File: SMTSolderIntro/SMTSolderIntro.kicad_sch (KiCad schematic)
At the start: 135 parts

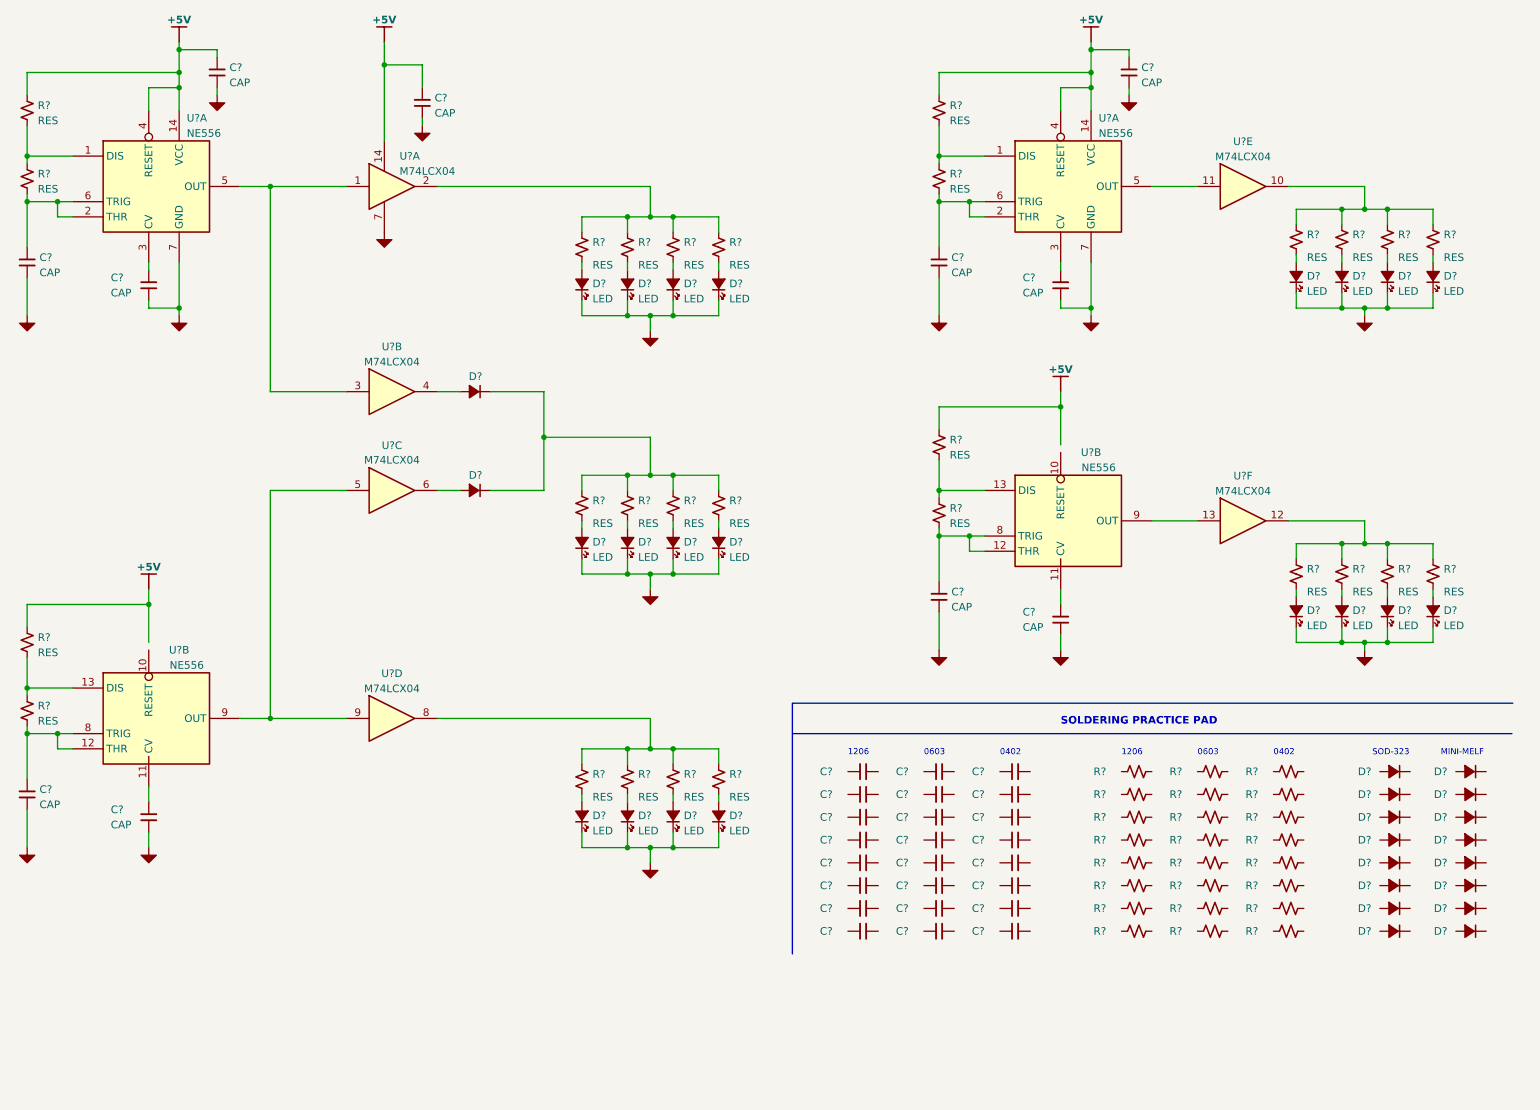
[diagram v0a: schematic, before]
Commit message: All components imported to board, nets still need work
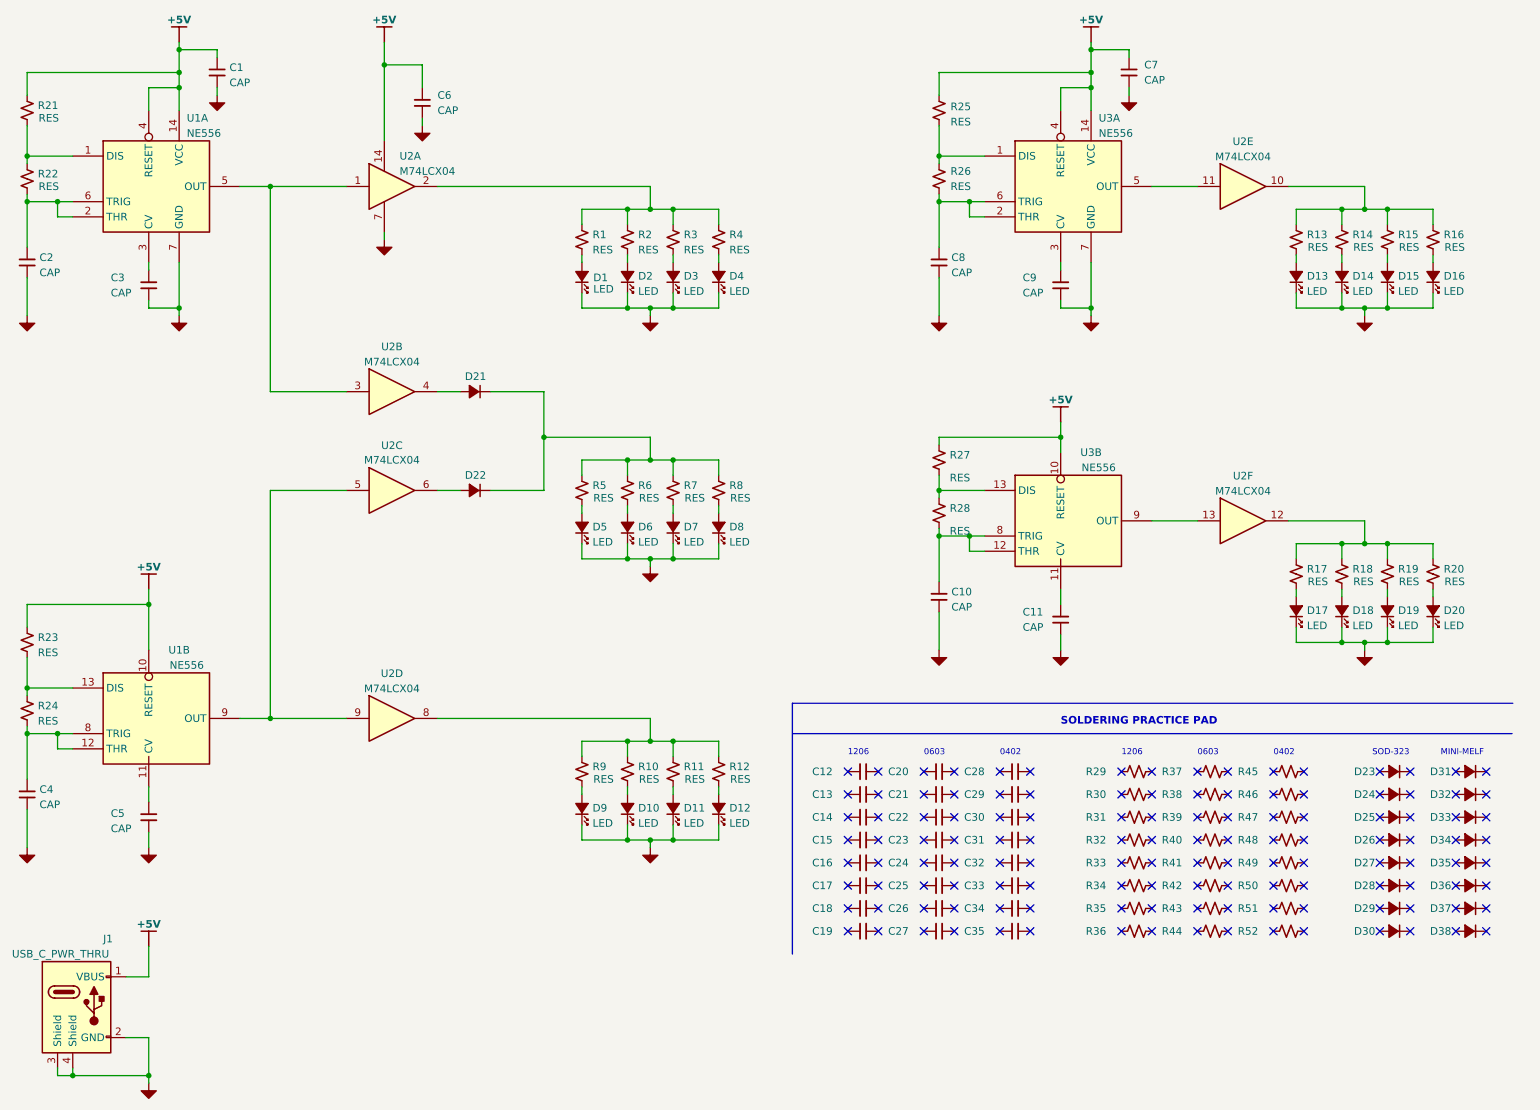
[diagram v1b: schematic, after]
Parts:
- removed D? (x2): DIODE, symbol Alpenglow:DIODE
- removed U? (x3): NE556, symbol Alpenglow:NE556
- added D21, D22: DIODE, Diode_SMD:D_MiniMELF_Handsoldering, symbol Alpenglow:DIODE
- added J1: USB_C_PWR_THRU, Alpenglow:USB_C_PWR_THRU, symbol Alpenglow:USB_C_PWR_THRU
- added U1: NE556, Alpenglow:SO-14, symbol Alpenglow:NE556
- added unit 2 of U3
- C1, C10, C11, C2, C3, C4, C5, C6, C7, C8, C9: renamed from C?; footprint (none) -> Capacitor_SMD:C_0805_2012Metric_Pad1.18x1.45mm_HandSolder
- C12, C13, C14, C15, C16, C17, C18, C19: renamed from C?; footprint (none) -> Capacitor_SMD:C_1206_3216Metric_Pad1.33x1.80mm_HandSolder
- C20, C21, C22, C23, C24, C25, C26, C27: renamed from C?; footprint (none) -> Capacitor_SMD:C_0603_1608Metric_Pad1.08x0.95mm_HandSolder
- C28, C29, C30, C31, C32, C33, C34, C35: renamed from C?; footprint (none) -> Capacitor_SMD:C_0402_1005Metric_Pad0.74x0.62mm_HandSolder
- D1, D10, D11, D12, D13, D14, D15, D16, D17, D18, D19, D2, D20, D3, D4, D5, D6, D7, D8, D9: renamed from D?; footprint (none) -> Alpenglow:LED_0805+; symbol Alpenglow:LED -> Alpenglow:LED_AK
- D23, D24, D25, D26, D27, D28, D29, D30: renamed from D?; footprint (none) -> Diode_SMD:D_SOD-323_HandSoldering
- D31, D32, D33, D34, D35, D36, D37, D38: renamed from D?; footprint (none) -> Diode_SMD:D_MiniMELF_Handsoldering
- R1, R10, R11, R12, R13, R14, R15, R16, R17, R18, R19, R2, R20, R21, R22, R23, R24, R25, R26, R27, R28, R3, R4, R5, R6, R7, R8, R9: renamed from R?; footprint (none) -> Resistor_SMD:R_0805_2012Metric_Pad1.20x1.40mm_HandSolder
- R29, R30, R31, R32, R33, R34, R35, R36: renamed from R?; footprint (none) -> Resistor_SMD:R_1206_3216Metric_Pad1.30x1.75mm_HandSolder
- R37, R38, R39, R40, R41, R42, R43, R44: renamed from R?; footprint (none) -> Resistor_SMD:R_0603_1608Metric_Pad0.98x0.95mm_HandSolder
- R45, R46, R47, R48, R49, R50, R51, R52: renamed from R?; footprint (none) -> Resistor_SMD:R_0402_1005Metric_Pad0.72x0.64mm_HandSolder
- U2: renamed from U?; footprint (none) -> Alpenglow:SO-16
- U3: renamed from U?; footprint (none) -> Alpenglow:SO-14
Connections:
- net +5V: now also C6.1, C7.1, R21.1, R25.1, R27.1, J1.1 (VBUS), U1.10 (RESET), U1.14 (VCC), U1.4 (RESET), U3.10 (RESET); no longer C2.1, C3.1, R1.1, R13.1, R2.1
- net GND: now also D1.K, D10.K, D11.K, D12.K, D13.K, D14.K, D15.K, D16.K, D17.K, D18.K, D19.K, D2.K, D20.K, D3.K, D4.K, D5.K, D6.K, D7.K, D8.K, D9.K, J1.2 (GND), J1.3 (Shield), J1.4 (Shield), U1.7 (GND); no longer D1.1 (K), D10.1 (K), D11.1 (K), D12.1 (K), D13.1 (K), D14.1 (K), D15.1 (K), D16.1 (K), D17.1 (K), D18.1 (K), D19.1 (K), D2.1 (K), D20.1 (K), D3.1 (K), D4.1 (K), D5.1 (K), D6.1 (K), D7.1 (K), D8.1 (K), D9.1 (K)
- net at U2.6: now also D22.A
- net at R14.1, R15.1, R16.1: now also R13.1, U2.10; no longer R17.1
- net at R19.1, R20.1, U2.12: now also R17.1, R18.1; no longer R21.1, R22.1
- net at R22.2: now also C2.1, U1.2 (THR), U1.6 (TRIG); no longer D16.2 (A)
- net at R17.2: now also D17.A; no longer D12.2 (A)
- net at R10.1, R11.1, R12.1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: now also U2.8; no longer U2.10
- net at R10.2: now also D10.A; no longer D6.2 (A)
- net at R21.2: now also R22.1, U1.1 (DIS); no longer D15.2 (A)
- net at U2.1, U2.3: now also U1.5 (OUT)
- net at R5.1, R6.1, R7.1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: now also D21.K, D22.K; no longer U2.2
- net at R12.2: now also D12.A; no longer D8.2 (A)
- net at U2.4: now also D21.A
- net at R15.2: now also D15.A; no longer D10.2 (A)
- net at U3.2 (THR), U3.6 (TRIG): now also C8.1, R26.2; no longer C5.1, R4.2
- net at U3.3 (CV): now also C9.1; no longer C7.1
- net at R24.2: now also C4.1, U1.12 (THR), U1.8 (TRIG); no longer C10.1
- net at R5.2: now also D5.A; no longer D1.2 (A)
- net at C11.1: now also U3.11 (CV)
- net at R23.2, R24.1: now also U1.13 (DIS)
- net at U2.5, U2.9: now also U1.9 (OUT)
- net at R11.2: now also D11.A; no longer D7.2 (A)
- net at R16.2: now also D16.A; no longer D11.2 (A)
- net at R9.2: now also D9.A; no longer D5.2 (A)
- net at R3.1: now also R1.1, R2.1, R4.1, U2.2; no longer R1.2
- net at R3.2: now also D3.A; no longer C4.1
- net at R20.2: now also D20.A; no longer D14.2 (A)
- net at R6.2: now also D6.A; no longer D2.2 (A)
- net at R18.2: now also D18.A; no longer C8.1
- net at R14.2: now also D14.A; no longer D9.2 (A)
- net at R28.2: now also C10.1, U3.12 (THR), U3.8 (TRIG); no longer D20.2 (A)
- net at R19.2: now also D19.A; no longer D13.2 (A)
- net at R13.2: now also D13.A; no longer R18.1
- net at R27.2: now also R28.1, U3.13 (DIS); no longer D19.2 (A)
- net at U2.13: now also U3.9 (OUT)
- net at R8.2: now also D8.A; no longer D4.2 (A)
- net at R7.2: now also D7.A; no longer D3.2 (A)
- net at R25.2: now also R26.1, U3.1 (DIS); no longer D17.2 (A)
- new net: D2.A, R2.2
- new net: C3.1, U1.3 (CV)
- new net: C5.1, U1.11 (CV)
- new net: D4.A, R4.2
- new net: D1.A, R1.2
- no-connect marks 0 -> 128
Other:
- moved on the sheet: C10, C11, C2, C3, C4, C5, C6, C7, C8, C9, D1, D10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

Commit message: fixed nets and components with bad footprints.  Ready for checking with printer.
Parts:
- D21, D22, D31, D32, D33, D34, D35, D36, D37, D38: footprint Diode_SMD:D_MiniMELF_Handsoldering -> Alpenglow:MINI_MELF
- D23, D24, D25, D26, D27, D28, D29, D30: footprint Diode_SMD:D_SOD-323_HandSoldering -> Alpenglow:SOD-323
- U2: footprint Alpenglow:SO-16 -> Alpenglow:SO-14

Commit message: Rough placement, added zip files to ignore
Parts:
- added D23, D24, D25, D26: DIODE, Alpenglow:SOD-323, symbol Alpenglow:DIODE
- added H1, H2, H3, H4: MountingHole_Pad, Alpenglow:MNTG-HOLE-BANANA, symbol Mechanical:MountingHole_Pad
- added J2: Barrel_Jack, Connector_BarrelJack:BarrelJack_CLIFF_FC681465S_SMT_Horizontal, symbol Connector:Barrel_Jack
- D21, D22: footprint Alpenglow:MINI_MELF -> Alpenglow:SOD-323
- renumbered D23 to D27, D24 to D28, D25 to D29, D26 to D30, D27 to D31, D28 to D32, D29 to D33, D30 to D34, D31 to D35, D32 to D36, D33 to D37, D34 to D38, D35 to D39, D36 to D40, D37 to D41, D38 to D42
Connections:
- net +5V: now also D23.K, D24.K, D25.K, D26.K; no longer J1.1 (VBUS)
- net GND: now also H1.1, H2.1, J2.2
- net BLINK1: now reaches R1.1, R2.1, R3.1, R4.1, U2.2
- net BLINK2: now reaches R10.1, R11.1, R12.1, R9.1, U2.8
- net CLK1: now reaches U1.5 (OUT), U2.1, U2.3
- net BLINK3: now reaches R13.1, R14.1, R15.1, R16.1, U2.10
- net CLK2: now reaches U1.9 (OUT), U2.5, U2.9
- net CLK3: now reaches U2.11, U3.5 (OUT)
- net BLINK5: now reaches D21.K, D22.K, R5.1, R6.1, R7.1, R8.1
- net BLINK4: now reaches R17.1, R18.1, R19.1, R20.1, U2.12
- net CLK4: now reaches U2.13, U3.9 (OUT)
- new net +Vbarrel: D26.A, J2.1
- new net +Vin_1: D23.A, H3.1
- new net +Vin_2: D24.A, H4.1
- new net +Vusb: D25.A, J1.1 (VBUS)
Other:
- note added: "MOUNTING HOLES / BANANA JACKS"
- moved on the sheet: J1

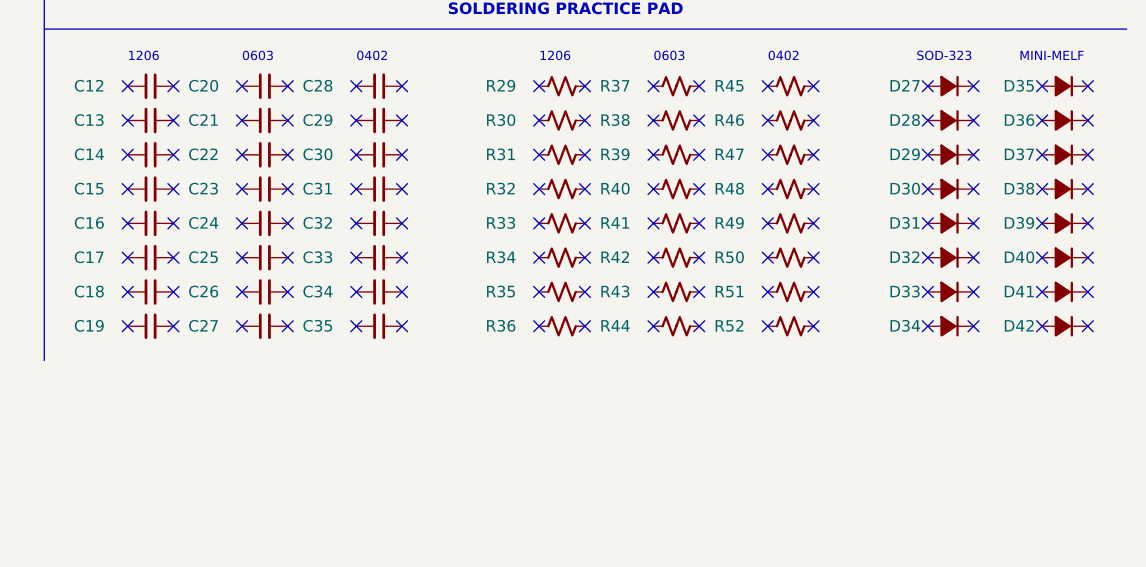
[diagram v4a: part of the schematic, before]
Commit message: Updated layout, Labeled practice component sizes, Added board name, Updated Schematic
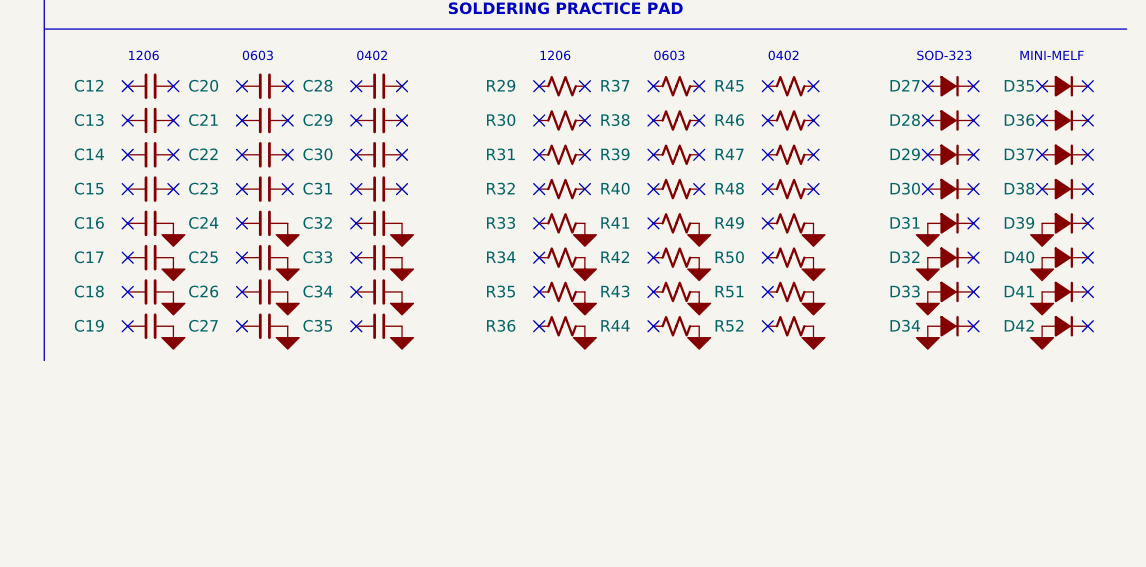
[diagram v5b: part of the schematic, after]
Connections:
- net GND: now also C16.2, C17.2, C18.2, C19.2, C24.2, C25.2, C26.2, C27.2, C32.2, C33.2, C34.2, C35.2, D31.A, D32.A, D33.A, D34.A, D39.A, D40.A, D41.A, D42.A, R33.2, R34.2, R35.2, R36.2, R41.2, R42.2, R43.2, R44.2, R49.2, R50.2, R51.2, R52.2
- no-connect marks 128 -> 96
